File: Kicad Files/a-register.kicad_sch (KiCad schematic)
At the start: 20 parts, among them U32 74LS245, U33 74LS173, U34 74LS173

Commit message: tidy up
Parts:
- renumbered C18 to C17, D79 to D63, D80 to D64, D81 to D65, D82 to D66, D83 to D67, D84 to D68, D85 to D69, D86 to D70, R88 to R72, R89 to R73, R90 to R74, R91 to R75, R92 to R76, R93 to R77, R94 to R78, R95 to R79, U32 to U26, U33 to U27, U34 to U28
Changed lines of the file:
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@@
   (symbol (lib_id "8bit-computer-rescue:74LS173-8bit-computer-rescue") (at 139.7 85.09 270) (unit 1)
     (in_bom yes) (on_board yes)
-    (property "Reference" "U33" (id 0) (at 142.24 87.63 0))
+    (property "Reference" "U27" (id 0) (at 142.24 87.63 0))
     (property "Value" "74LS173" (id 1) (at 138.43 87.63 0))
     (property "Footprint" "Package_DIP:DIP-16_W7.62mm" (id 2) (at 139.7 85.09 0)
@@
   (symbol (lib_id "8bit-computer-rescue:LED_ALT-Device") (at 120.65 158.75 90) (unit 1)
     (in_bom yes) (on_board yes)
-    (property "Reference" "D81" (id 0) (at 118.11 158.75 0))
+    (property "Reference" "D65" (id 0) (at 118.11 158.75 0))
     (property "Value" "RED" (id 1) (at 123.19 158.75 0))
     (property "Footprint" "LED_THT:LED_D5.0mm" (id 2) (at 120.65 158.75 0)
@@
   (symbol (lib_id "8bit-computer-rescue:LED_ALT-Device") (at 151.13 158.75 90) (unit 1)
     (in_bom yes) (on_board yes)
-    (property "Reference" "D85" (id 0) (at 148.59 158.75 0))
+    (property "Reference" "D69" (id 0) (at 148.59 158.75 0))
     (property "Value" "RED" (id 1) (at 153.67 158.75 0))
     (property "Footprint" "LED_THT:LED_D5.0mm" (id 2) (at 151.13 158.75 0)
@@
   (symbol (lib_id "8bit-computer-rescue:LED_ALT-Device") (at 158.75 158.75 90) (unit 1)
     (in_bom yes) (on_board yes)
-    (property "Reference" "D86" (id 0) (at 156.21 158.75 0))
+    (property "Reference" "D70" (id 0) (at 156.21 158.75 0))
     (property "Value" "RED" (id 1) (at 161.29 158.75 0))
     (property "Footprint" "LED_THT:LED_D5.0mm" (id 2) (at 158.75 158.75 0)
@@
   (symbol (lib_id "Device:R") (at 120.65 170.18 0) (unit 1)
     (in_bom yes) (on_board yes)
-    (property "Reference" "R90" (id 0) (at 122.682 170.18 90))
+    (property "Reference" "R74" (id 0) (at 122.682 170.18 90))
     (property "Value" "R" (id 1) (at 120.65 170.18 90))
     (property "Footprint" "Resistor_THT:R_Axial_DIN0207_L6.3mm_D2.5mm_P7.62mm_Horizontal" (id 2) (at 118.872 170.18 90)
@@
   (symbol (lib_id "Device:R") (at 128.27 170.18 0) (unit 1)
     (in_bom yes) (on_board yes)
-    (property "Reference" "R91" (id 0) (at 130.302 170.18 90))
+    (property "Reference" "R75" (id 0) (at 130.302 170.18 90))
     (property "Value" "R" (id 1) (at 128.27 170.18 90))
     (property "Footprint" "Resistor_THT:R_Axial_DIN0207_L6.3mm_D2.5mm_P7.62mm_Horizontal" (id 2) (at 126.492 170.18 90)
@@
   (symbol (lib_id "Device:R") (at 143.51 170.18 0) (unit 1)
     (in_bom yes) (on_board yes)
-    (property "Reference" "R93" (id 0) (at 145.542 170.18 90))
+    (property "Reference" "R77" (id 0) (at 145.542 170.18 90))
     (property "Value" "R" (id 1) (at 143.51 170.18 90))
     (property "Footprint" "Resistor_THT:R_Axial_DIN0207_L6.3mm_D2.5mm_P7.62mm_Horizontal" (id 2) (at 141.732 170.18 90)
@@
   (symbol (lib_id "Device:R") (at 158.75 170.18 0) (unit 1)
     (in_bom yes) (on_board yes)
-    (property "Reference" "R95" (id 0) (at 160.782 170.18 90))
+    (property "Reference" "R79" (id 0) (at 160.782 170.18 90))
     (property "Value" "R" (id 1) (at 158.75 170.18 90))
     (property "Footprint" "Resistor_THT:R_Axial_DIN0207_L6.3mm_D2.5mm_P7.62mm_Horizontal" (id 2) (at 156.972 170.18 90)
@@
   (symbol (lib_id "power:VCC") (at 107.95 102.87 180) (unit 1)
     (in_bom yes) (on_board yes)
-    (property "Reference" "#PWR075" (id 0) (at 107.95 99.06 0)
+    (property "Reference" "#PWR058" (id 0) (at 107.95 99.06 0)
       (effects (font (size 1.27 1.27)) hide)
     )
@@
   (symbol (lib_id "8bit-computer-rescue:74LS173-8bit-computer-rescue") (at 180.34 85.09 270) (unit 1)
     (in_bom yes) (on_board yes)
-    (property "Reference" "U34" (id 0) (at 182.88 87.63 0))
+    (property "Reference" "U28" (id 0) (at 182.88 87.63 0))
     (property "Value" "74LS173" (id 1) (at 179.07 87.63 0))
     (property "Footprint" "Package_DIP:DIP-16_W7.62mm" (id 2) (at 180.34 85.09 0)
@@
   (symbol (lib_id "8bit-computer-rescue:74LS245-8bit-computer-rescue") (at 97.79 85.09 90) (unit 1)
     (in_bom yes) (on_board yes)
-    (property "Reference" "U32" (id 0) (at 83.185 82.55 0)
+    (property "Reference" "U26" (id 0) (at 83.185 82.55 0)
       (effects (font (size 1.27 1.27)) (justify left bottom))
     )
@@
   (symbol (lib_id "8bit-computer-rescue:LED_ALT-Device") (at 105.41 158.75 90) (unit 1)
     (in_bom yes) (on_board yes)
-    (property "Reference" "D79" (id 0) (at 102.87 158.75 0))
+    (property "Reference" "D63" (id 0) (at 102.87 158.75 0))
     (property "Value" "RED" (id 1) (at 107.95 158.75 0))
     (property "Footprint" "LED_THT:LED_D5.0mm" (id 2) (at 105.41 158.75 0)
@@
   (symbol (lib_id "8bit-computer-rescue:LED_ALT-Device") (at 113.03 158.75 90) (unit 1)
     (in_bom yes) (on_board yes)
-    (property "Reference" "D80" (id 0) (at 110.49 158.75 0))
+    (property "Reference" "D64" (id 0) (at 110.49 158.75 0))
     (property "Value" "RED" (id 1) (at 115.57 158.75 0))
     (property "Footprint" "LED_THT:LED_D5.0mm" (id 2) (at 113.03 158.75 0)
@@
   (symbol (lib_id "8bit-computer-rescue:LED_ALT-Device") (at 128.27 158.75 90) (unit 1)
     (in_bom yes) (on_board yes)
-    (property "Reference" "D82" (id 0) (at 125.73 158.75 0))
+    (property "Reference" "D66" (id 0) (at 125.73 158.75 0))
     (property "Value" "RED" (id 1) (at 130.81 158.75 0))
     (property "Footprint" "LED_THT:LED_D5.0mm" (id 2) (at 128.27 158.75 0)
@@
   (symbol (lib_id "8bit-computer-rescue:LED_ALT-Device") (at 135.89 158.75 90) (unit 1)
     (in_bom yes) (on_board yes)
-    (property "Reference" "D83" (id 0) (at 133.35 158.75 0))
+    (property "Reference" "D67" (id 0) (at 133.35 158.75 0))
     (property "Value" "RED" (id 1) (at 138.43 158.75 0))
     (property "Footprint" "LED_THT:LED_D5.0mm" (id 2) (at 135.89 158.75 0)
@@
   (symbol (lib_id "8bit-computer-rescue:LED_ALT-Device") (at 143.51 158.75 90) (unit 1)
     (in_bom yes) (on_board yes)
-    (property "Reference" "D84" (id 0) (at 140.97 158.75 0))
+    (property "Reference" "D68" (id 0) (at 140.97 158.75 0))
     (property "Value" "RED" (id 1) (at 146.05 158.75 0))
     (property "Footprint" "LED_THT:LED_D5.0mm" (id 2) (at 143.51 158.75 0)
@@
   (symbol (lib_id "Device:R") (at 105.41 170.18 0) (unit 1)
     (in_bom yes) (on_board yes)
-    (property "Reference" "R88" (id 0) (at 107.442 170.18 90))
+    (property "Reference" "R72" (id 0) (at 107.442 170.18 90))
     (property "Value" "R" (id 1) (at 105.41 170.18 90))
     (property "Footprint" "Resistor_THT:R_Axial_DIN0207_L6.3mm_D2.5mm_P7.62mm_Horizontal" (id 2) (at 103.632 170.18 90)
@@
   (symbol (lib_id "Device:R") (at 113.03 170.18 0) (unit 1)
     (in_bom yes) (on_board yes)
-    (property "Reference" "R89" (id 0) (at 115.062 170.18 90))
+    (property "Reference" "R73" (id 0) (at 115.062 170.18 90))
     (property "Value" "R" (id 1) (at 113.03 170.18 90))
     (property "Footprint" "Resistor_THT:R_Axial_DIN0207_L6.3mm_D2.5mm_P7.62mm_Horizontal" (id 2) (at 111.252 170.18 90)
@@
   (symbol (lib_id "Device:R") (at 135.89 170.18 0) (unit 1)
     (in_bom yes) (on_board yes)
-    (property "Reference" "R92" (id 0) (at 137.922 170.18 90))
+    (property "Reference" "R76" (id 0) (at 137.922 170.18 90))
     (property "Value" "R" (id 1) (at 135.89 170.18 90))
     (property "Footprint" "Resistor_THT:R_Axial_DIN0207_L6.3mm_D2.5mm_P7.62mm_Horizontal" (id 2) (at 134.112 170.18 90)
@@
   (symbol (lib_id "Device:R") (at 151.13 170.18 0) (unit 1)
     (in_bom yes) (on_board yes)
-    (property "Reference" "R94" (id 0) (at 153.162 170.18 90))
+    (property "Reference" "R78" (id 0) (at 153.162 170.18 90))
     (property "Value" "R" (id 1) (at 151.13 170.18 90))
     (property "Footprint" "Resistor_THT:R_Axial_DIN0207_L6.3mm_D2.5mm_P7.62mm_Horizontal" (id 2) (at 149.352 170.18 90)
@@
   (symbol (lib_id "power:GND") (at 132.08 182.88 0) (unit 1)
     (in_bom yes) (on_board yes)
-    (property "Reference" "#PWR076" (id 0) (at 132.08 189.23 0)
+    (property "Reference" "#PWR059" (id 0) (at 132.08 189.23 0)
       (effects (font (size 1.27 1.27)) hide)
     )
@@
   (symbol (lib_id "power:GND") (at 201.93 72.39 0) (unit 1)
     (in_bom yes) (on_board yes)
-    (property "Reference" "#PWR077" (id 0) (at 201.93 78.74 0)
+    (property "Reference" "#PWR060" (id 0) (at 201.93 78.74 0)
       (effects (font (size 1.27 1.27)) hide)
     )
@@
   (symbol (lib_id "Device:C") (at 237.49 83.82 0) (unit 1)
     (in_bom yes) (on_board yes)
-    (property "Reference" "C18" (id 0) (at 238.125 81.28 0)
+    (property "Reference" "C17" (id 0) (at 238.125 81.28 0)
       (effects (font (size 1.27 1.27)) (justify left))
     )
@@
   (symbol (lib_id "power:GND") (at 237.49 90.17 0) (unit 1)
     (in_bom yes) (on_board yes)
-    (property "Reference" "#PWR079" (id 0) (at 237.49 96.52 0)
+    (property "Reference" "#PWR062" (id 0) (at 237.49 96.52 0)
       (effects (font (size 1.27 1.27)) hide)
     )
@@
   (symbol (lib_id "power:VCC") (at 237.49 77.47 0) (unit 1)
     (in_bom yes) (on_board yes)
-    (property "Reference" "#PWR078" (id 0) (at 237.49 81.28 0)
-      (effects (font (size 1.27 1.27)) hide)
-    )
+    (property "Reference" "#PWR061" (id 0) (at 237.49 81.28 0)
+      (effects (font (size 1.27 1.27)) hide)
+    )

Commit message: updated library
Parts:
- removed D63, D64, D65, D66, D67, D68, D69, D70: RED, LED_THT:LED_D5.0mm, symbol 8bit-computer-rescue:LED_ALT-Device
- removed R72, R73, R74, R75, R76, R77, R78, R79: R, Resistor_THT:R_Axial_DIN0207_L6.3mm_D2.5mm_P7.62mm_Horizontal, symbol Device:R
- removed U26: 74LS245, Package_DIP:DIP-20_W7.62mm, symbol 8bit-computer-rescue:74LS245-8bit-computer-rescue
- removed U27, U28: 74LS173, Package_DIP:DIP-16_W7.62mm, symbol 8bit-computer-rescue:74LS173-8bit-computer-rescue
- added D71, D72, D73, D74, D75, D76, D77, D78: LED, symbol Device:LED
- added R80, R81, R82, R83, R84, R85, R86, R87: R_Small, symbol Device:R_Small
- added U26: 74HC245, symbol 74xx:74HC245
- added U27, U28: 74LS173, symbol 74xx:74LS173
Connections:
- net A_0: now also D78.2 (A), U26.9 (A7), U28.6 (Q3)
- net A_1: now also D77.2 (A), U26.8 (A6), U28.5 (Q2)
- net A_2: now also D76.2 (A), U26.7 (A5), U28.4 (Q1)
- net A_3: now also D75.2 (A), U26.6 (A4), U28.3 (Q0)
- net A_4: now also D74.2 (A), U26.5 (A3), U27.6 (Q3)
- net A_5: now also D73.2 (A), U26.4 (A2), U27.5 (Q2)
- net A_6: now also D72.2 (A), U26.3 (A1), U27.4 (Q1)
- net A_7: now also D71.2 (A), U26.2 (A0), U27.3 (Q0)
- net BUS_0: now also U26.11 (B7), U28.11 (D3)
- net BUS_1: now also U26.12 (B6), U28.12 (D2)
- net BUS_2: now also U26.13 (B5), U28.13 (D1)
- net BUS_3: now also U26.14 (B4), U28.14 (D0)
- net BUS_4: now also U26.15 (B3), U27.11 (D3)
- net BUS_5: now also U26.16 (B2), U27.12 (D2)
- net BUS_6: now also U26.17 (B1), U27.13 (D1)
- net BUS_7: now also U26.18 (B0), U27.14 (D0)
- net CLK: now also U27.7 (Cp), U28.7 (Cp)
- net CLR: now also U27.15 (Mr), U28.15 (Mr)
- net GND: now also R80.2, R81.2, R82.2, R83.2, R84.2, R85.2, R86.2, R87.2, U26.10 (GND), U27.1 (Oe1), U27.16 (VCC), U27.2 (Oe2), U28.1 (Oe1), U28.16 (VCC), U28.2 (Oe2)
- net VCC: now also U26.1 (A->B), U26.20 (VCC), U27.8 (GND), U28.8 (GND)
- net ~{AI}: now also U27.10 (E2), U27.9 (E1), U28.10 (E2), U28.9 (E1)
- net ~{AO}: now also U26.19 (CE)
- new net: D74.1 (K), R83.1
- new net: D73.1 (K), R82.1
- new net: D76.1 (K), R85.1
- new net: D71.1 (K), R80.1
- new net: D77.1 (K), R86.1
- new net: D72.1 (K), R81.1
- new net: D75.1 (K), R84.1
- new net: D78.1 (K), R87.1
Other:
- moved on the sheet: C17

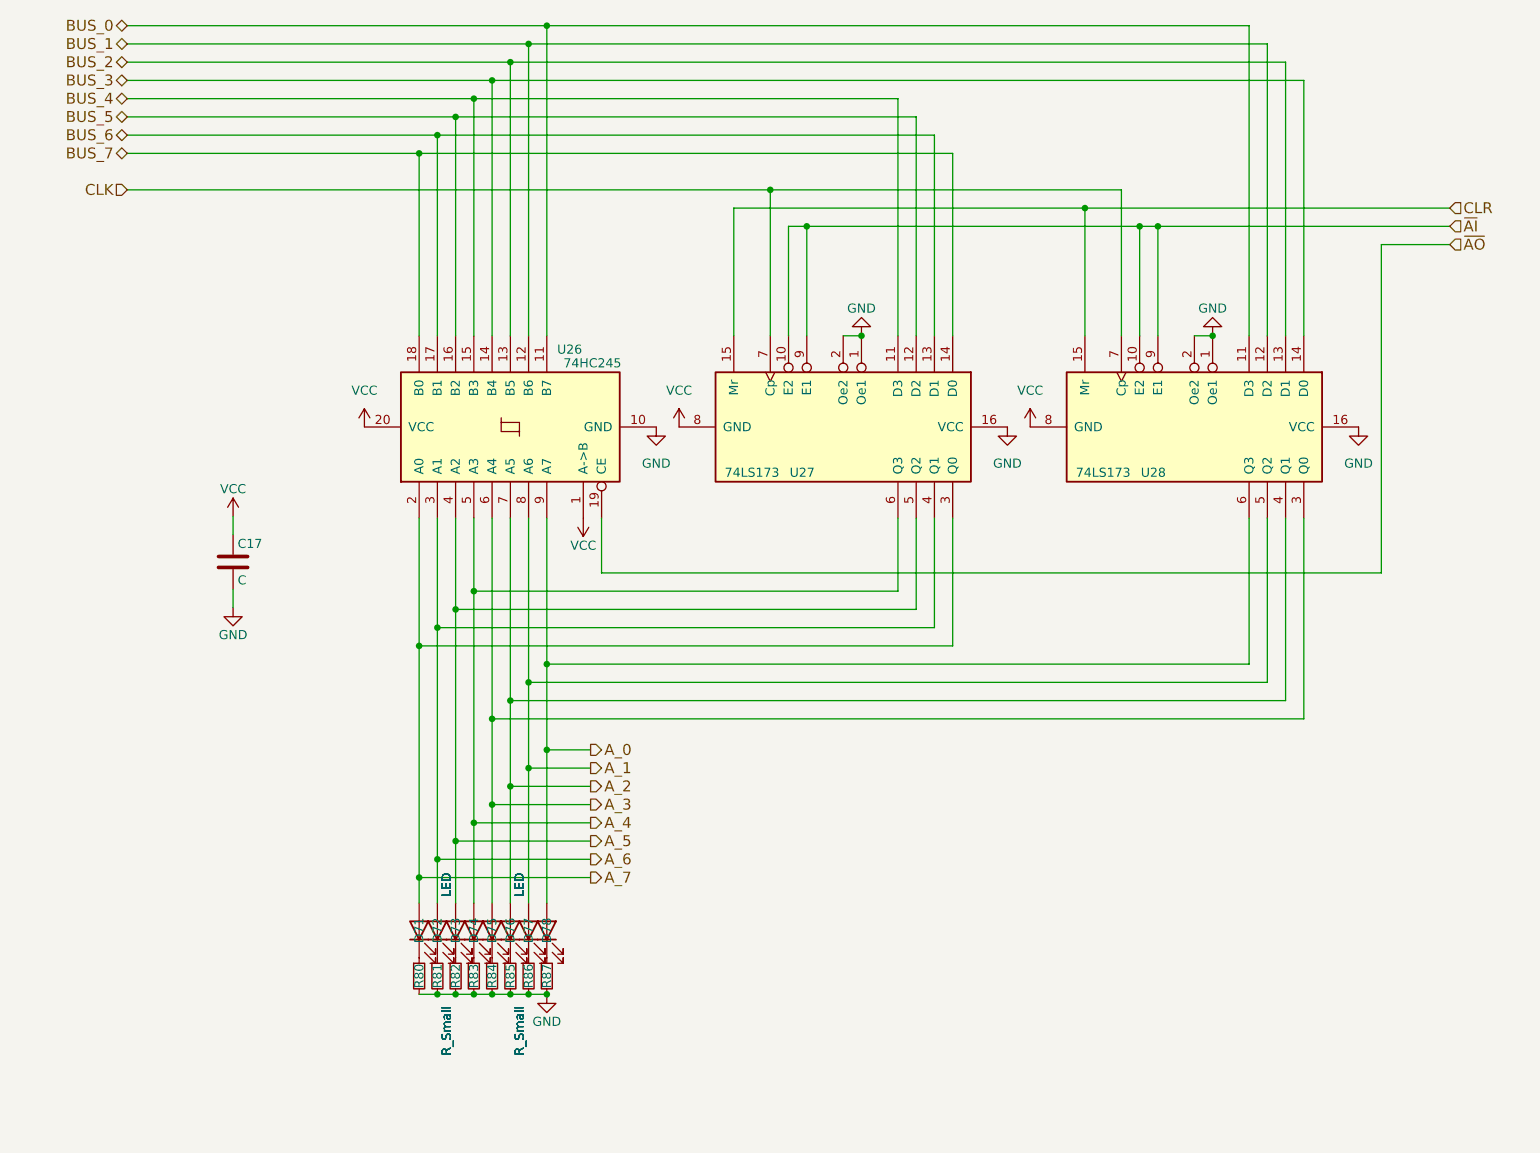
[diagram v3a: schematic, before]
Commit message: complete redraw to bus system
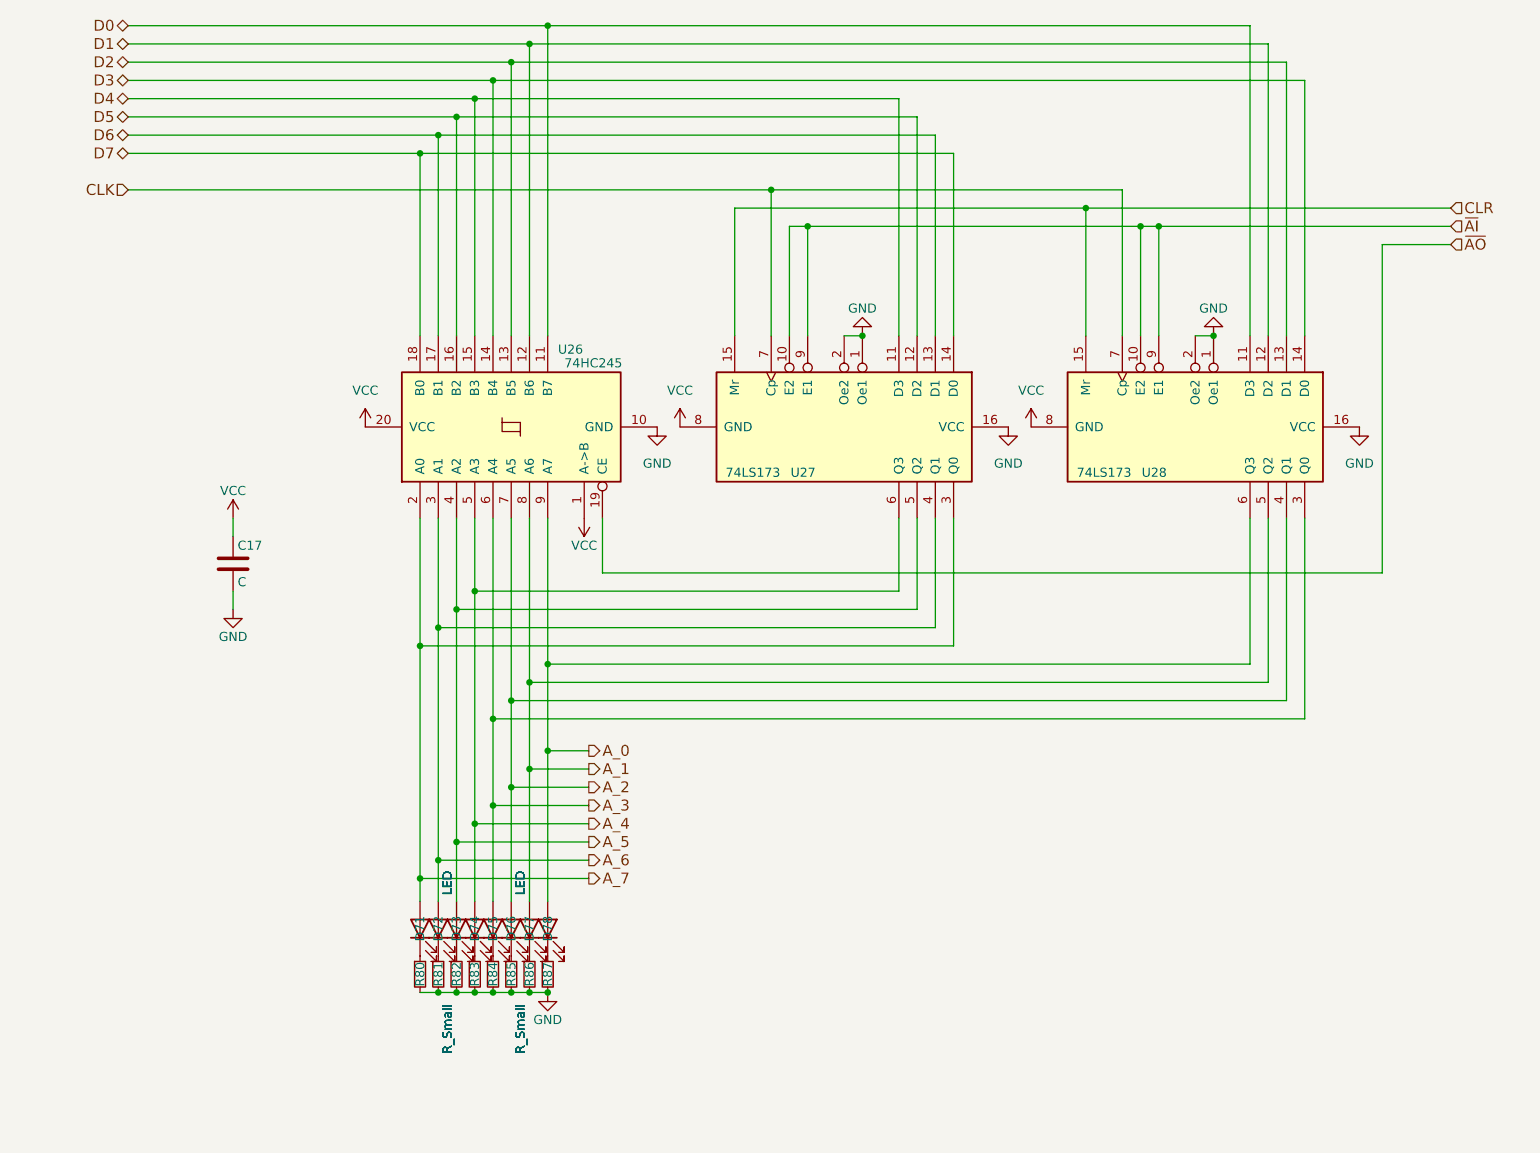
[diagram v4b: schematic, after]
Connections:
- net BUS_0 renamed D0
- net BUS_1 renamed D1
- net BUS_2 renamed D2
- net BUS_3 renamed D3
- net BUS_4 renamed D4
- net BUS_5 renamed D5
- net BUS_6 renamed D6
- net BUS_7 renamed D7
